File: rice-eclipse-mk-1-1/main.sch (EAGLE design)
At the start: 53 parts, among them U1 LM1084ISX-5.0/NOPB, U2 THS4531IDRD8-M, U3 THS4531IDRD8-M, U4 THS4531IDRD8-M, U5 THS4531IDRD8-M, X1 2540-5

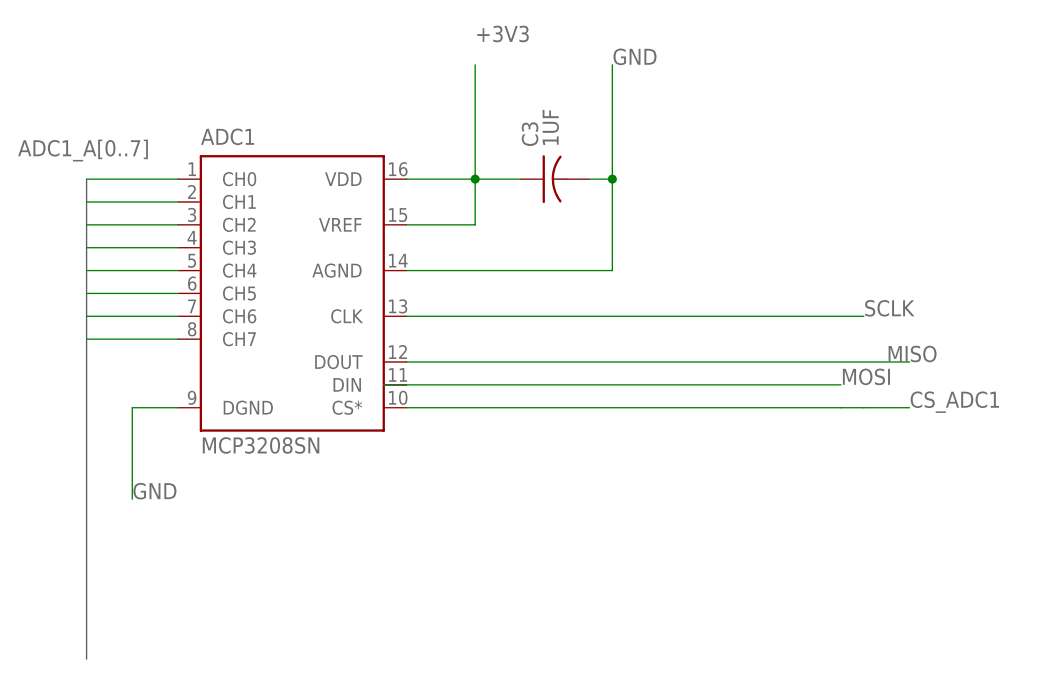
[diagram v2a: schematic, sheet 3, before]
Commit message: Added RPI GPIO connections.
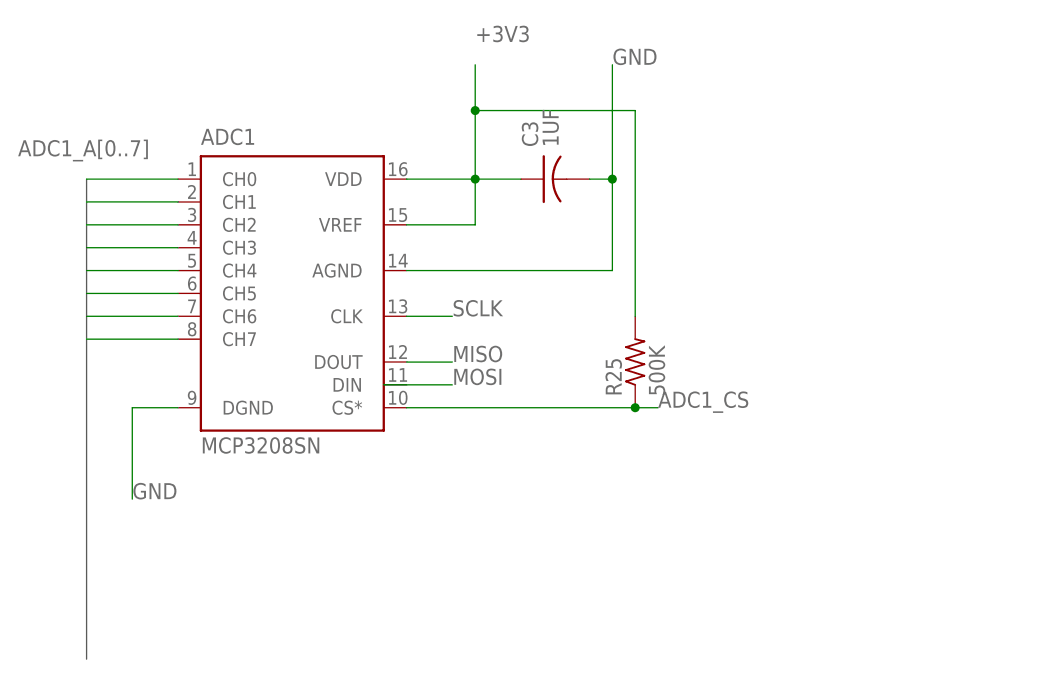
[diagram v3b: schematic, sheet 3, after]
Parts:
- added R25: 500K, rcl:R-US_R0603
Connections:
- net RPI_GPIO_19 renamed MOSI
- net RPI_GPIO_21 renamed MISO
- net RPI_GPIO_23 renamed SCLK
- net RPI_GPIO_24 renamed ADC2_CS
- net RPI_GPIO_26 renamed ADC3_CS
- removed net RPI_GPIO_11: X1-11.KL
- removed net RPI_GPIO_13: X1-13.KL
- removed net RPI_GPIO_15: X1-15.KL
- removed net RPI_GPIO_16: X1-16.KL
- removed net RPI_GPIO_2: X1-2.KL
- removed net RPI_GPIO_22: X1-22.KL
- removed net RPI_GPIO_6: X1-6.KL
- new net ADC1_CS: R25.1, X1-22.KL
- net +3V3: now also R25.2
- net +5V: now also X1-2.KL
- net CTRL_SOLENOID_1: now also X1-11.KL
- net CTRL_SOLENOID_2: now also X1-13.KL
- net CTRL_SOLENOID_3: now also X1-15.KL
- net GND: now also X1-6.KL
- net IGNITION_RELAY: now also X1-16.KL
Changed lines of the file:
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@@
 <part name="R24" library="rcl" library_urn="urn:adsk.eagle:library:334" deviceset="R-US_" device="R0603" package3d_urn="urn:adsk.eagle:package:23555/2" value="20K"/>
 <part name="C13" library="resistor" library_urn="urn:adsk.eagle:library:348" deviceset="C-US" device="C0603" package3d_urn="urn:adsk.eagle:package:26138/1" value="1UF"/>
+<part name="R25" library="rcl" library_urn="urn:adsk.eagle:library:334" deviceset="R-US_" device="R0603" package3d_urn="urn:adsk.eagle:package:23555/2" value="500K"/>
 </parts>
 <sheets>
@@
 <attribute name="VALUE" x="100.711" y="102.616" size="1.778" layer="96" rot="R90"/>
 </instance>
+<instance part="R25" gate="G$1" x="109.22" y="78.74" rot="R90"/>
 </instances>
 <busses>
@@
 <pinref part="ADC1" gate="P" pin="VDD"/>
 <wire x1="91.44" y1="93.98" x2="91.44" y2="99.06" width="0.1524" layer="91"/>
-<wire x1="91.44" y1="99.06" x2="91.44" y2="111.76" width="0.1524" layer="91"/>
+<wire x1="91.44" y1="99.06" x2="91.44" y2="106.68" width="0.1524" layer="91"/>
+<wire x1="91.44" y1="106.68" x2="91.44" y2="111.76" width="0.1524" layer="91"/>
 <wire x1="83.82" y1="99.06" x2="91.44" y2="99.06" width="0.1524" layer="91"/>
 <junction x="91.44" y="99.06"/>
@@
 <pinref part="C3" gate="G$1" pin="1"/>
 <wire x1="91.44" y1="99.06" x2="96.52" y2="99.06" width="0.1524" layer="91"/>
+<pinref part="R25" gate="G$1" pin="2"/>
+<wire x1="109.22" y1="83.82" x2="109.22" y2="106.68" width="0.1524" layer="91"/>
+<wire x1="109.22" y1="106.68" x2="91.44" y2="106.68" width="0.1524" layer="91"/>
+<junction x="91.44" y="106.68"/>
 </segment>
 </net>
 <net name="SCLK" class="0">
 <segment>
-<wire x1="83.82" y1="83.82" x2="134.62" y2="83.82" width="0.1524" layer="91"/>
-<label x="134.62" y="83.82" size="1.778" layer="95"/>
+<wire x1="83.82" y1="83.82" x2="88.9" y2="83.82" width="0.1524" layer="91"/>
+<label x="88.9" y="83.82" size="1.778" layer="95"/>
 </segment>
 </net>
 <net name="MISO" class="0">
 <segment>
-<wire x1="83.82" y1="78.74" x2="139.7" y2="78.74" width="0.1524" layer="91"/>
-<label x="137.16" y="78.74" size="1.778" layer="95"/>
+<wire x1="83.82" y1="78.74" x2="88.9" y2="78.74" width="0.1524" layer="91"/>
+<label x="88.9" y="78.74" size="1.778" layer="95"/>
 </segment>
 </net>
 <net name="MOSI" class="0">
 <segment>
-<wire x1="81.28" y1="76.2" x2="132.08" y2="76.2" width="0.1524" layer="91"/>
-<label x="132.08" y="76.2" size="1.778" layer="95"/>
-</segment>
-</net>
-<net name="CS_ADC1" class="0">
-<segment>
-<wire x1="83.82" y1="73.66" x2="132.08" y2="73.66" width="0.1524" layer="91"/>
-<label x="139.7" y="73.66" size="1.778" layer="95"/>
-<wire x1="132.08" y1="73.66" x2="134.62" y2="73.66" width="0.1524" layer="91"/>
-<wire x1="134.62" y1="73.66" x2="139.7" y2="73.66" width="0.1524" layer="91"/>
+<wire x1="81.28" y1="76.2" x2="88.9" y2="76.2" width="0.1524" layer="91"/>
+<label x="88.9" y="76.2" size="1.778" layer="95"/>
+</segment>
+</net>
+<net name="ADC1_CS" class="0">
+<segment>
+<wire x1="83.82" y1="73.66" x2="109.22" y2="73.66" width="0.1524" layer="91"/>
+<label x="111.76" y="73.66" size="1.778" layer="95"/>
+<wire x1="109.22" y1="73.66" x2="111.76" y2="73.66" width="0.1524" layer="91"/>
+<pinref part="R25" gate="G$1" pin="1"/>
+<junction x="109.22" y="73.66"/>
 </segment>
 </net>
@@
 </segment>
 </net>
-<net name="RPI_GPIO_2" class="0">
-<segment>
-<pinref part="X1" gate="-2" pin="KL"/>
-<wire x1="195.58" y1="53.34" x2="185.42" y2="53.34" width="0.1524" layer="91"/>
-</segment>
-</net>
 <net name="RPI_GPIO_3" class="0">
 <segment>
@@
 </segment>
 </net>
-<net name="RPI_GPIO_6" class="0">
-<segment>
-<pinref part="X1" gate="-6" pin="KL"/>
-<wire x1="195.58" y1="63.5" x2="185.42" y2="63.5" width="0.1524" layer="91"/>
-</segment>
-</net>
 <net name="RPI_GPIO_7" class="0">
 <segment>
@@
 </segment>
 </net>
-<net name="RPI_GPIO_8" class="0">
-<segment>
-<pinref part="X1" gate="-8" pin="KL"/>
-<wire x1="195.58" y1="68.58" x2="185.42" y2="68.58" width="0.1524" layer="91"/>
-</segment>
-</net>
 <net name="RPI_GPIO_40" class="0">
 <segment>
@@
 </segment>
 </net>
-<net name="RPI_GPIO_26" class="0">
+<net name="ADC3_CS" class="0">
 <segment>
 <pinref part="X1" gate="-26" pin="KL"/>
 <wire x1="195.58" y1="114.3" x2="185.42" y2="114.3" width="0.1524" layer="91"/>
+<label x="185.42" y="114.3" size="1.778" layer="95"/>
 </segment>
 </net>
@@
 </segment>
 </net>
-<net name="RPI_GPIO_24" class="0">
-<segment>
-<pinref part="X1" gate="-24" pin="KL"/>
-<wire x1="195.58" y1="109.22" x2="185.42" y2="109.22" width="0.1524" layer="91"/>
-</segment>
-</net>
-<net name="RPI_GPIO_23" class="0">
+<net name="SCLK" class="0">
 <segment>
 <pinref part="X1" gate="-23" pin="KL"/>
 <wire x1="195.58" y1="106.68" x2="185.42" y2="106.68" width="0.1524" layer="91"/>
-</segment>
-</net>
-<net name="RPI_GPIO_22" class="0">
+<label x="185.42" y="106.68" size="1.778" layer="95"/>
+</segment>
+</net>
+<net name="ADC1_CS" class="0">
 <segment>
 <pinref part="X1" gate="-22" pin="KL"/>
 <wire x1="195.58" y1="104.14" x2="185.42" y2="104.14" width="0.1524" layer="91"/>
-</segment>
-</net>
-<net name="RPI_GPIO_21" class="0">
+<label x="185.42" y="104.14" size="1.778" layer="95"/>
+</segment>
+</net>
+<net name="MISO" class="0">
 <segment>
 <pinref part="X1" gate="-21" pin="KL"/>
 <wire x1="195.58" y1="101.6" x2="185.42" y2="101.6" width="0.1524" layer="91"/>
+<label x="185.42" y="101.6" size="1.778" layer="95"/>
 </segment>
 </net>
@@
 </segment>
 </net>
-<net name="RPI_GPIO_19" class="0">
+<net name="MOSI" class="0">
 <segment>
 <pinref part="X1" gate="-19" pin="KL"/>
 <wire x1="195.58" y1="96.52" x2="185.42" y2="96.52" width="0.1524" layer="91"/>
+<label x="185.42" y="96.52" size="1.778" layer="95"/>
 </segment>
 </net>
@@
 </segment>
 </net>
-<net name="RPI_GPIO_16" class="0">
+<net name="IGNITION_RELAY" class="0">
 <segment>
 <pinref part="X1" gate="-16" pin="KL"/>
 <wire x1="195.58" y1="88.9" x2="185.42" y2="88.9" width="0.1524" layer="91"/>
-</segment>
-</net>
-<net name="RPI_GPIO_15" class="0">
+<label x="185.42" y="88.9" size="1.778" layer="95"/>
+</segment>
+</net>
+<net name="CTRL_SOLENOID_3" class="0">
 <segment>
 <pinref part="X1" gate="-15" pin="KL"/>
 <wire x1="195.58" y1="86.36" x2="185.42" y2="86.36" width="0.1524" layer="91"/>
+<label x="185.42" y="86.36" size="1.778" layer="95"/>
 </segment>
 </net>
@@
 </segment>
 </net>
-<net name="RPI_GPIO_13" class="0">
+<net name="CTRL_SOLENOID_2" class="0">
 <segment>
 <pinref part="X1" gate="-13" pin="KL"/>
 <wire x1="195.58" y1="81.28" x2="185.42" y2="81.28" width="0.1524" layer="91"/>
-</segment>
-</net>
-<net name="RPI_GPIO_11" class="0">
+<label x="185.42" y="81.28" size="1.778" layer="95"/>
+</segment>
+</net>
+<net name="CTRL_SOLENOID_1" class="0">
 <segment>
 <pinref part="X1" gate="-11" pin="KL"/>
 <wire x1="195.58" y1="76.2" x2="185.42" y2="76.2" width="0.1524" layer="91"/>
+<label x="185.42" y="76.2" size="1.778" layer="95"/>
 </segment>
 </net>
@@
 <label x="86.36" y="154.94" size="1.778" layer="95"/>
 </segment>
+<segment>
+<pinref part="X1" gate="-2" pin="KL"/>
+<wire x1="195.58" y1="53.34" x2="185.42" y2="53.34" width="0.1524" layer="91"/>
+<label x="185.42" y="53.34" size="1.778" layer="95"/>
+</segment>
 </net>
 <net name="GND" class="0">
@@
 <label x="86.36" y="152.4" size="1.778" layer="95"/>
 </segment>
+<segment>
+<pinref part="X1" gate="-6" pin="KL"/>
+<wire x1="195.58" y1="63.5" x2="185.42" y2="63.5" width="0.1524" layer="91"/>
+<label x="185.42" y="63.5" size="1.778" layer="95"/>
+</segment>
 </net>
 <net name="RELAY_NEGATIVE" class="0">
@@
 </segment>
 </net>
+<net name="RPI_GPIO_8" class="0">
+<segment>
+<pinref part="X1" gate="-8" pin="KL"/>
+<wire x1="195.58" y1="68.58" x2="185.42" y2="68.58" width="0.1524" layer="91"/>
+</segment>
+</net>
+<net name="ADC2_CS" class="0">
+<segment>
+<pinref part="X1" gate="-24" pin="KL"/>
+<wire x1="195.58" y1="109.22" x2="185.42" y2="109.22" width="0.1524" layer="91"/>
+<label x="185.42" y="109.22" size="1.778" layer="95"/>
+</segment>
+</net>

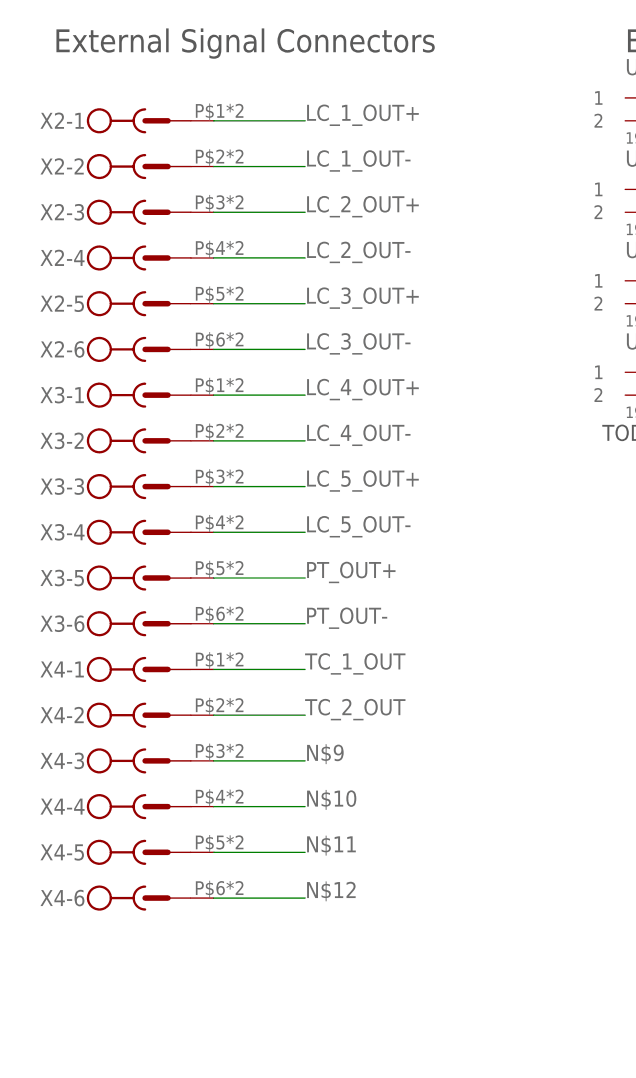
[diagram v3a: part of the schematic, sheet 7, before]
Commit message: EAGLE stuff
- changed 6 pin connectors to 4 pin for loadcells 1-4
- deleted load cell 5 connector
- added debugging slide switches
- board rearranged
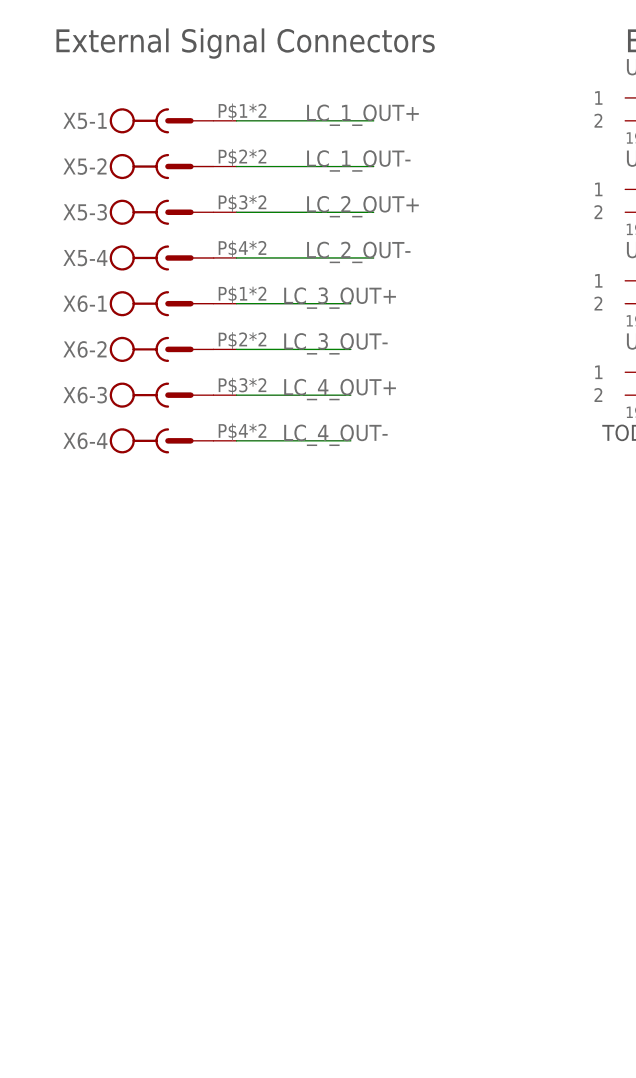
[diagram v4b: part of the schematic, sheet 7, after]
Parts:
- removed X2, X3, X4: (no value), con-phoenix-250-extra:1770924
- added U$10, U$11, U$12: SLIDE_SW, SLIDE_SW:SLIDE_SW
- added X5, X6: (no value), con-phoenix-250-extra:1770908
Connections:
- removed net LC_5_OUT+: X3-3.SK
- removed net LC_5_OUT-: X3-4.SK
- removed net N$10: X4-4.SK
- removed net N$11: X4-5.SK
- removed net N$12: X4-6.SK
- removed net N$9: X4-3.SK
- removed net PT_OUT+: X3-5.SK
- removed net PT_OUT-: X3-6.SK
- removed net TC_1_OUT: X4-1.SK
- removed net TC_2_OUT: X4-2.SK
- new net DEBUG_3V3: U$11.P$1
- new net DEBUG_5V: U$12.P$3
- net +12V: now also U$10.P$2, U$10.P$3
- net +3V3: now also U$11.P$3
- net +5V: now also U$12.P$2
- net LC_1_OUT+: now also X5-1.SK; no longer X2-1.SK
- net LC_1_OUT-: now also X5-2.SK; no longer X2-2.SK
- net LC_2_OUT+: now also X5-3.SK; no longer X2-3.SK
- net LC_2_OUT-: now also X5-4.SK; no longer X2-4.SK
- net LC_3_OUT+: now also X6-1.SK; no longer X2-5.SK
- net LC_3_OUT-: now also X6-2.SK; no longer X2-6.SK
- net LC_4_OUT+: now also X6-3.SK; no longer X3-1.SK
- net LC_4_OUT-: now also X6-4.SK; no longer X3-2.SK
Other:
- moved on the sheet: U$1G$1

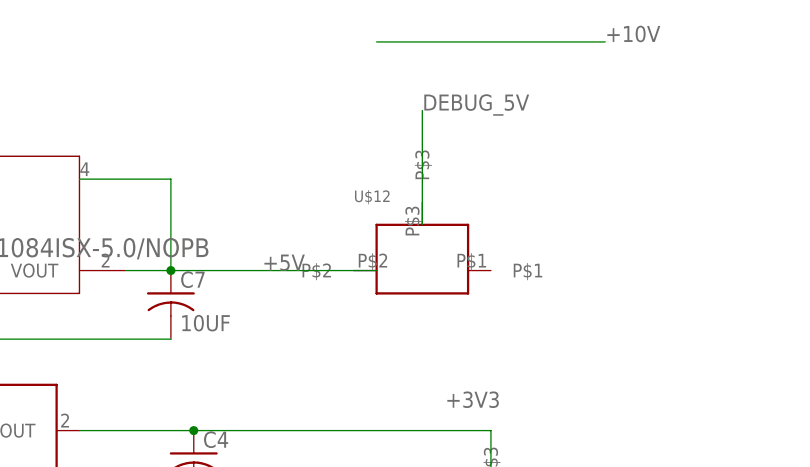
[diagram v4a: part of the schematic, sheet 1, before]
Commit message: Eagle Stuff
changed 5v_debug to 5v
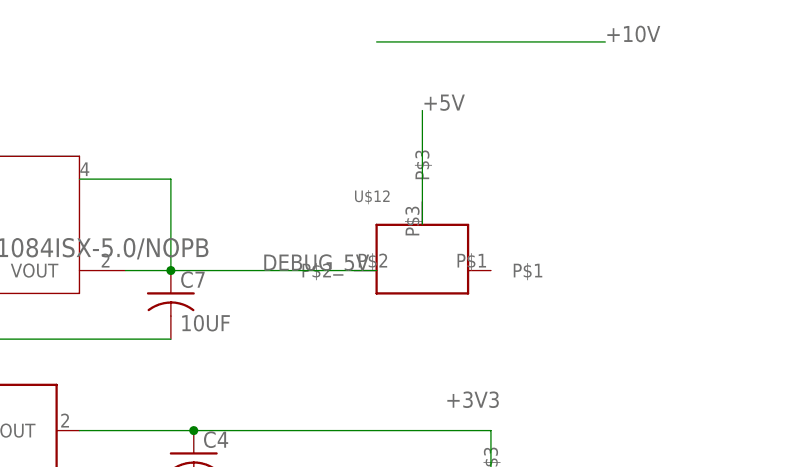
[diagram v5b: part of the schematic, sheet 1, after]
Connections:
- net +5V: now also U$12.P$3; no longer C7.1, U$12.P$2, U1.4, U1.VOUT
- net DEBUG_5V: now also C7.1, U$12.P$2, U1.4, U1.VOUT; no longer U$12.P$3
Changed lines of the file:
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@@
 <net name="+5V" class="0">
+<segment>
+<pinref part="U$12" gate="G$1" pin="P$3"/>
+<wire x1="198.12" y1="116.84" x2="198.12" y2="129.54" width="0.1524" layer="91"/>
+<label x="198.12" y="129.54" size="1.778" layer="95"/>
+</segment>
+</net>
+<net name="+10V" class="0">
+<segment>
+<wire x1="193.04" y1="137.16" x2="218.44" y2="137.16" width="0.1524" layer="91"/>
+<label x="218.44" y="137.16" size="1.778" layer="95"/>
+</segment>
+</net>
+<net name="DEBUG_3V3" class="0">
+<segment>
+<pinref part="U$11" gate="G$1" pin="P$1"/>
+<wire x1="210.82" y1="78.74" x2="228.6" y2="78.74" width="0.1524" layer="91"/>
+<label x="228.6" y="78.74" size="1.778" layer="95"/>
+</segment>
+</net>
+<net name="DEBUG_5V" class="0">
 <segment>
 <label x="180.34" y="111.76" size="1.778" layer="95"/>
@@
 </segment>
 </net>
-<net name="+10V" class="0">
-<segment>
-<wire x1="193.04" y1="137.16" x2="218.44" y2="137.16" width="0.1524" layer="91"/>
-<label x="218.44" y="137.16" size="1.778" layer="95"/>
-</segment>
-</net>
-<net name="DEBUG_5V" class="0">
-<segment>
-<pinref part="U$12" gate="G$1" pin="P$3"/>
-<wire x1="198.12" y1="116.84" x2="198.12" y2="129.54" width="0.1524" layer="91"/>
-<label x="198.12" y="129.54" size="1.778" layer="95"/>
-</segment>
-</net>
-<net name="DEBUG_3V3" class="0">
-<segment>
-<pinref part="U$11" gate="G$1" pin="P$1"/>
-<wire x1="210.82" y1="78.74" x2="228.6" y2="78.74" width="0.1524" layer="91"/>
-<label x="228.6" y="78.74" size="1.778" layer="95"/>
-</segment>
-</net>
